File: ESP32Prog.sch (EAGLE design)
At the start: 18 parts, among them T1 MMBT2222, T2 MMBT2222, U1 3.3V, U3 CH340C

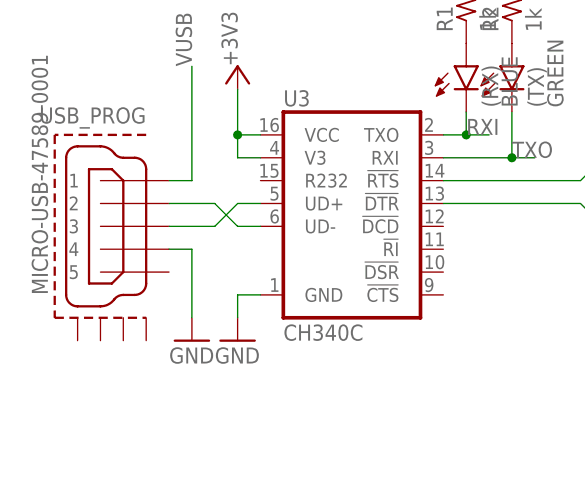
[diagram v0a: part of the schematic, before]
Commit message: fixed gnd pin
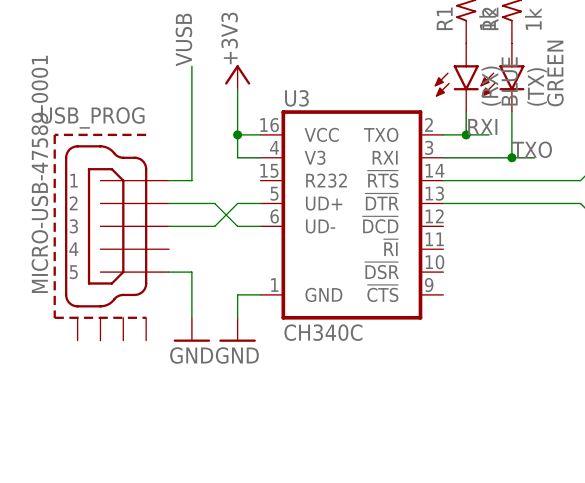
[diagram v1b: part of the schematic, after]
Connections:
- net GND: now also USB_PROG.5; no longer USB_PROG.4
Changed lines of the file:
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@@
 <?xml version="1.0" encoding="utf-8"?>
 <!DOCTYPE eagle SYSTEM "eagle.dtd">
-<eagle version="9.6.1">
+<eagle version="9.6.2">
 <drawing>
 <settings>
@@
 </segment>
 <segment>
-<pinref part="USB_PROG" gate="G$1" pin="4"/>
-<wire x1="-35.56" y1="40.64" x2="-33.02" y2="40.64" width="0.1524" layer="91"/>
 <pinref part="GND7" gate="1" pin="GND"/>
-<wire x1="-33.02" y1="40.64" x2="-33.02" y2="33.02" width="0.1524" layer="91"/>
-</segment>
-<segment>
+<pinref part="USB_PROG" gate="G$1" pin="5"/>
+<wire x1="-33.02" y1="38.1" x2="-33.02" y2="33.02" width="0.1524" layer="91"/>
+<wire x1="-33.02" y1="38.1" x2="-35.56" y2="38.1" width="0.1524" layer="91"/>
+</segment>
+<segment>
